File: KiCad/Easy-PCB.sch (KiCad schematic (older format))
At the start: 1 part, among them J3 HLW20R-2C7LF

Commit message: microcontroller schematic kicad
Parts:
- added C?: 0.1u, symbol C_Small
- added P?: USART, symbol CONN_01X02
- added P?: CONN_01X06, symbol CONN_01X06
- added R? (x8): 320, symbol R
- added R? (x4): 10k, symbol R
- added U?: PIC16F883, symbol PIC16F883
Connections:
- net Heat Relay/DoorC1: now also J3.19 (P19)
- net Heat Relay/DoorC2: now also J3.20 (P20)
- net Heat Relay/Heat: now also U?.5 (RA3/AN3/Vref+/C1IN+)
- net Temperature Feedback/Tk: now also U?.2 (RA0/AN0/ULPWU/C12IN0-)
- net Temperature Feedback/Tref: now also U?.3 (RA1/AN1/C12IN1-)
- net Temperature Feedback/Vref-: now also U?.4 (RA2/AN2/Vref-/CVref/C2IN+)
- net CS1: now reaches J3.1 (P1)
- net CS1: now also R?.2, U?.7 (RA5/AN4/~SS~/C2OUT)
- net VDD: now reaches J3.10 (P10)
- net VDD: now also J3.8 (P8), J3.9 (P9), C?.2, P?.2 (P2), R?.1, R?.1, R?.1, R?.1, U?.20 (Vdd)
- net at J3.11 (P11): now also R?.2
- net at J3.12 (P12): now also R?.2
- net at J3.13 (P13): now also R?.2
- net at J3.14 (P14): now also R?.2
- net at J3.15 (P15): now also R?.2
- net at J3.16 (P16): now also R?.2
- net at J3.17 (P17): now also R?.2
- net at J3.18 (P18): now also R?.2
- net SCK: now reaches J3.2 (P2)
- net SCK: now also R?.2, U?.14 (RC3/SCK/SCL)
- net MISO: now reaches J3.3 (P3)
- net MISO: now also U?.15 (RC4/SDI/SDA)
- net MOSI: now reaches J3.4 (P4)
- net MOSI: now also U?.16 (RC5/SDO)
- net GND: now reaches J3.5 (P5)
- net GND: now also J3.6 (P6), J3.7 (P7), C?.1, P?.3 (P3), U?.19 (Vss), U?.8 (Vss)
- new net: P?.1 (P1), U?.1 (RE3/~MCLR~/Vpp)
- new net: R?.1, U?.21 (RB0/AN12/INT)
- new net: R?.1, U?.22 (RB1/AN10/P1C/C12IN3-)
- new net: R?.1, U?.23 (RB2/AN8/P1B)
- new net: R?.1, U?.24 (RB3/AN9/PGM/C12IN2-)
- new net: R?.1, U?.25 (RB4/AN11/P1D)
- new net: R?.1, U?.26 (RB5/AN13/~T1G)
- new net: P?.5 (P5), R?.1, U?.27 (RB6/ICSPCLK)
- new net: P?.4 (P4), R?.1, U?.28 (RB7/ICSPDAT)
- new net CS2: R?.2, U?.10 (RA6/OSC2/CLKOUT)
- new net RX: P?.2 (P2), U?.18 (RC7/RX/DT)
- new net TX: P?.1 (P1), U?.17 (RC6/TX/CK)
- no-connect marks 0 -> 1
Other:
- moved on the sheet: J3

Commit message: kicad motor and speaker schematics
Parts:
- added Q?: 2N3904, SOT-23, symbol MMBT3904
- added R? (x2): 1k, symbol R
- added SP?: SPEAKER, symbol SPEAKER
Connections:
- net GND: now also Q?.2 (E)
- net VDD: now also R?.1, SP?.1
- net Motor Driver/Motor_On: now reaches U?.11 (RC0/T1OSO/T1CKI)
- net Motor Driver/wind2: now reaches U?.12 (RC1/T1OSI/CCP2)
- net Motor Driver/wind1: now reaches U?.13 (RC2/P1A/CCP1)
- net at U?.6 (RA4/T0CLI/C1OUT): now also R?.2
- new net: Q?.3 (C), R?.2, SP?.2
- new net: Q?.1 (B), R?.1
- no-connect marks 1 -> 2
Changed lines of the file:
@@
 $Descr USLetter 11000 8500
 encoding utf-8
-Sheet 1 3
+Sheet 1 4
 Title "Easy-PCB-v1"
 Date ""
@@
 	-1   0    0    1
 $EndComp
-Wire Wire Line
-	1600 3600 1200 3600
-Wire Wire Line
-	1600 3700 1200 3700
-Wire Wire Line
-	1600 3800 1200 3800
-Wire Wire Line
-	1200 3900 1600 3900
-Wire Wire Line
-	1200 4000 1600 4000
-Wire Wire Line
-	1200 4100 1600 4100
-Wire Wire Line
-	1200 4200 1600 4200
-Wire Wire Line
-	1200 4300 1600 4300
-Wire Wire Line
-	1900 3700 2800 3700
-Wire Wire Line
-	1900 3800 2800 3800
-Wire Wire Line
-	1900 3900 2800 3900
-Wire Wire Line
-	1900 4000 2800 4000
-Wire Wire Line
-	1900 4100 2800 4100
-Wire Wire Line
-	1900 4200 2800 4200
-Wire Wire Line
-	1900 4300 2800 4300
-Wire Wire Line
-	1900 3600 2700 3600
-Wire Wire Line
-	2700 3600 2700 3500
-Wire Wire Line
-	2700 3500 2800 3500
-Wire Wire Line
-	1200 2900 1500 2900
-Wire Wire Line
-	1500 2900 1500 3000
-Wire Wire Line
-	1500 3000 2800 3000
-Wire Wire Line
-	1200 3100 2150 3100
-Wire Wire Line
-	1300 3500 1200 3500
-Wire Wire Line
-	1300 3300 1300 3500
-Connection ~ 1300 3400
-Wire Wire Line
-	1300 3300 1200 3300
-Wire Wire Line
-	1300 3200 1200 3200
-Wire Wire Line
-	1300 3000 1300 3200
-Connection ~ 1300 3100
-Wire Wire Line
-	1200 3000 1300 3000
-Wire Wire Line
-	2800 3300 2150 3300
-Wire Wire Line
-	2150 3300 2150 3100
-Connection ~ 2000 3100
-Wire Wire Line
-	1200 3400 2800 3400
-Connection ~ 1500 3400
-Wire Wire Line
-	1700 3150 1700 3100
-Connection ~ 1700 3100
-Wire Wire Line
-	1700 3350 1700 3400
-Connection ~ 1700 3400
-Wire Wire Line
-	1200 2800 1900 2800
-Wire Wire Line
-	1900 2800 1900 2900
-Wire Wire Line
-	1900 2900 2800 2900
-Wire Wire Line
-	2600 2000 2600 3200
-Wire Wire Line
-	2600 3200 2800 3200
-Wire Wire Line
-	2500 2000 2500 3100
-Wire Wire Line
-	2500 3100 2800 3100
-Wire Wire Line
-	5300 3500 5450 3500
-Wire Wire Line
-	5600 3700 5300 3700
-Wire Wire Line
-	5600 2200 5600 3700
-Wire Wire Line
-	5600 2600 1200 2600
-Wire Wire Line
-	1200 2700 5300 2700
-Wire Wire Line
-	5300 2200 5300 2900
-Wire Wire Line
-	5300 4200 5800 4200
-Wire Wire Line
-	5300 4100 5700 4100
-Wire Wire Line
-	5300 4000 5600 4000
-Wire Wire Line
-	5600 4000 5600 5600
-Wire Wire Line
-	5600 5600 6300 5600
-Wire Wire Line
-	5700 4100 5700 5500
-Wire Wire Line
-	5700 5500 6300 5500
-Wire Wire Line
-	5800 4200 5800 5400
-Wire Wire Line
-	5800 5400 6300 5400
-Wire Wire Line
-	8100 4600 1500 4600
-Wire Wire Line
-	1500 4600 1500 4400
-Wire Wire Line
-	1500 4400 1200 4400
-Wire Wire Line
-	8100 4700 1200 4700
-Wire Wire Line
-	1200 4700 1200 4500
-Wire Wire Line
-	5300 3900 6100 3900
-Wire Wire Line
-	6100 3900 6100 4450
-Wire Wire Line
-	6100 4450 8100 4450
-Wire Wire Line
-	6300 5900 5150 5900
-Wire Wire Line
-	6300 6050 5150 6050
-Wire Wire Line
-	5300 3300 5900 3300
-Wire Wire Line
-	5900 2200 5900 5750
-Wire Wire Line
-	5900 5750 6300 5750
-Connection ~ 5300 2700
-Connection ~ 5600 2600
-Connection ~ 5900 3300
-Wire Wire Line
-	5300 1900 5300 1800
-Wire Wire Line
-	5300 1800 5900 1800
-Wire Wire Line
-	5900 1800 5900 1900
-Wire Wire Line
-	5600 1650 5600 1900
-Connection ~ 5600 1800
-Wire Wire Line
-	2400 2050 2500 2050
-Connection ~ 2500 2050
-Wire Wire Line
-	2600 2050 2700 2050
-Connection ~ 2600 2050
-Wire Wire Line
-	2800 5500 5300 5500
-Wire Wire Line
-	5300 5500 5300 4300
-Connection ~ 3300 5500
-Wire Wire Line
-	3300 5050 3300 5150
-Wire Wire Line
-	2700 5500 2700 5100
-Wire Wire Line
-	2700 5100 3300 5100
-Connection ~ 3300 5100
-Wire Wire Line
-	2600 5500 2600 5300
 $Comp
 L CONN_01X06 P?
@@
 $EndComp
 NoConn ~ 2300 5500
+$Comp
+L SPEAKER SP?
+U 1 1 56815E3D
+P 7550 3600
+F 0 "SP?" H 7450 3850 50  0000 C CNN
+F 1 "SPEAKER" H 7450 3350 50  0000 C CNN
+F 2 "" H 7550 3600 50  0000 C CNN
+F 3 "" H 7550 3600 50  0000 C CNN
+	1    7550 3600
+	1    0    0    -1
+$EndComp
+$Comp
+L MMBT3904 Q?
+U 1 1 56815FFA
+P 6900 4000
+F 0 "Q?" H 7100 4075 50  0000 L CNN
+F 1 "2N3904" H 7100 4000 50  0000 L CNN
+F 2 "SOT-23" H 7100 3925 50  0000 L CIN
+F 3 "" H 6900 4000 50  0000 L CNN
+	1    6900 4000
+	1    0    0    -1
+$EndComp
+$Comp
+L R R?
+U 1 1 56816949
+P 6800 3600
+F 0 "R?" V 6880 3600 50  0000 C CNN
+F 1 "1k" V 6800 3600 50  0000 C CNN
+F 2 "" V 6730 3600 50  0000 C CNN
+F 3 "" H 6800 3600 50  0000 C CNN
+	1    6800 3600
+	1    0    0    -1
+$EndComp
+$Comp
+L R R?
+U 1 1 568169CA
+P 6350 3800
+F 0 "R?" V 6430 3800 50  0000 C CNN
+F 1 "1k" V 6350 3800 50  0000 C CNN
+F 2 "" V 6280 3800 50  0000 C CNN
+F 3 "" H 6350 3800 50  0000 C CNN
+	1    6350 3800
+	0    1    1    0
+$EndComp
+$Comp
+L GND #PWR?
+U 1 1 56816B80
+P 7000 4200
+F 0 "#PWR?" H 7000 3950 50  0001 C CNN
+F 1 "GND" H 7000 4050 50  0000 C CNN
+F 2 "" H 7000 4200 50  0000 C CNN
+F 3 "" H 7000 4200 50  0000 C CNN
+	1    7000 4200
+	1    0    0    -1
+$EndComp
+$Comp
+L VDD #PWR?
+U 1 1 56816C00
+P 7000 3450
+F 0 "#PWR?" H 7000 3300 50  0001 C CNN
+F 1 "VDD" H 7000 3600 50  0000 C CNN
+F 2 "" H 7000 3450 50  0000 C CNN
+F 3 "" H 7000 3450 50  0000 C CNN
+	1    7000 3450
+	1    0    0    -1
+$EndComp
+Wire Wire Line
+	1600 3600 1200 3600
+Wire Wire Line
+	1600 3700 1200 3700
+Wire Wire Line
+	1600 3800 1200 3800
+Wire Wire Line
+	1200 3900 1600 3900
+Wire Wire Line
+	1200 4000 1600 4000
+Wire Wire Line
+	1200 4100 1600 4100
+Wire Wire Line
+	1200 4200 1600 4200
+Wire Wire Line
+	1200 4300 1600 4300
+Wire Wire Line
+	1900 3700 2800 3700
+Wire Wire Line
+	1900 3800 2800 3800
+Wire Wire Line
+	1900 3900 2800 3900
+Wire Wire Line
+	1900 4000 2800 4000
+Wire Wire Line
+	1900 4100 2800 4100
+Wire Wire Line
+	1900 4200 2800 4200
+Wire Wire Line
+	1900 4300 2800 4300
+Wire Wire Line
+	1900 3600 2700 3600
+Wire Wire Line
+	2700 3600 2700 3500
+Wire Wire Line
+	2700 3500 2800 3500
+Wire Wire Line
+	1200 2900 1500 2900
+Wire Wire Line
+	1500 2900 1500 3000
+Wire Wire Line
+	1500 3000 2800 3000
+Wire Wire Line
+	1200 3100 2150 3100
+Wire Wire Line
+	1300 3500 1200 3500
+Wire Wire Line
+	1300 3300 1300 3500
+Connection ~ 1300 3400
+Wire Wire Line
+	1300 3300 1200 3300
+Wire Wire Line
+	1300 3200 1200 3200
+Wire Wire Line
+	1300 3000 1300 3200
+Connection ~ 1300 3100
+Wire Wire Line
+	1200 3000 1300 3000
+Wire Wire Line
+	2800 3300 2150 3300
+Wire Wire Line
+	2150 3300 2150 3100
+Connection ~ 2000 3100
+Wire Wire Line
+	1200 3400 2800 3400
+Connection ~ 1500 3400
+Wire Wire Line
+	1700 3150 1700 3100
+Connection ~ 1700 3100
+Wire Wire Line
+	1700 3350 1700 3400
+Connection ~ 1700 3400
+Wire Wire Line
+	1200 2800 1900 2800
+Wire Wire Line
+	1900 2800 1900 2900
+Wire Wire Line
+	1900 2900 2800 2900
+Wire Wire Line
+	2600 2000 2600 3200
+Wire Wire Line
+	2600 3200 2800 3200
+Wire Wire Line
+	2500 2000 2500 3100
+Wire Wire Line
+	2500 3100 2800 3100
+Wire Wire Line
+	5300 3500 5450 3500
+Wire Wire Line
+	5600 3700 5300 3700
+Wire Wire Line
+	5600 2200 5600 3700
+Wire Wire Line
+	5600 2600 1200 2600
+Wire Wire Line
+	1200 2700 5300 2700
+Wire Wire Line
+	5300 2200 5300 2900
+Wire Wire Line
+	5300 4200 5800 4200
+Wire Wire Line
+	5300 4100 5700 4100
+Wire Wire Line
+	5300 4000 5600 4000
+Wire Wire Line
+	5600 4000 5600 5600
+Wire Wire Line
+	5600 5600 6300 5600
+Wire Wire Line
+	5700 4100 5700 5500
+Wire Wire Line
+	5700 5500 6300 5500
+Wire Wire Line
+	5800 4200 5800 5400
+Wire Wire Line
+	5800 5400 6300 5400
+Wire Wire Line
+	8100 4600 1500 4600
+Wire Wire Line
+	1500 4600 1500 4400
+Wire Wire Line
+	1500 4400 1200 4400
+Wire Wire Line
+	8100 4700 1200 4700
+Wire Wire Line
+	1200 4700 1200 4500
+Wire Wire Line
+	5300 3900 6100 3900
+Wire Wire Line
+	6100 3900 6100 4450
+Wire Wire Line
+	6100 4450 8100 4450
+Wire Wire Line
+	6300 5900 5150 5900
+Wire Wire Line
+	6300 6050 5150 6050
+Wire Wire Line
+	5300 3300 5900 3300
+Wire Wire Line
+	5900 2200 5900 5750
+Wire Wire Line
+	5900 5750 6300 5750
+Connection ~ 5300 2700
+Connection ~ 5600 2600
+Connection ~ 5900 3300
+Wire Wire Line
+	5300 1900 5300 1800
+Wire Wire Line
+	5300 1800 5900 1800
+Wire Wire Line
+	5900 1800 5900 1900
+Wire Wire Line
+	5600 1650 5600 1900
+Connection ~ 5600 1800
+Wire Wire Line
+	2400 2050 2500 2050
+Connection ~ 2500 2050
+Wire Wire Line
+	2600 2050 2700 2050
+Connection ~ 2600 2050
+Wire Wire Line
+	2800 5500 5300 5500
+Wire Wire Line
+	5300 5500 5300 4300
+Connection ~ 3300 5500
+Wire Wire Line
+	3300 5050 3300 5150
+Wire Wire Line
+	2700 5500 2700 5100
+Wire Wire Line
+	2700 5100 3300 5100
+Connection ~ 3300 5100
+Wire Wire Line
+	2600 5500 2600 5300
 Wire Wire Line
 	2400 5500 2400 4200
@@
 	2500 5500 2500 4300
 Connection ~ 2500 4300
+Wire Wire Line
+	6800 3450 7000 3450
+Wire Wire Line
+	7000 3450 7000 3500
+Wire Wire Line
+	7000 3500 7250 3500
+Wire Wire Line
+	6800 3750 7000 3750
+Wire Wire Line
+	7000 3700 7000 3800
+Wire Wire Line
+	7000 3700 7250 3700
+Connection ~ 7000 3750
+Wire Wire Line
+	5300 3800 6200 3800
+Wire Wire Line
+	6500 3800 6600 3800
+Wire Wire Line
+	6600 3800 6600 4000
+Wire Wire Line
+	6600 4000 6700 4000
+$Sheet
+S 8100 2900 1000 500
+U 5681BEC8
+F0 "Motor Driver" 60
+F1 "Motor-Driver.sch" 60
+F2 "wind1a" O R 9100 3000 60
+F3 "wind1b" O R 9100 3100 60
+F4 "wind2a" O R 9100 3200 60
+F5 "wind2b" O R 9100 3300 60
+F6 "wind1" I L 8100 3000 60
+F7 "wind2" I L 8100 3100 60
+F8 "Motor_On" I L 8100 3200 60
+$EndSheet
+Wire Wire Line
+	5300 3200 8100 3200
+Wire Wire Line
+	5300 3100 8100 3100
+Wire Wire Line
+	5300 3000 8100 3000
+NoConn ~ 5300 3400
 $EndSCHEMATC

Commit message: power circuit schematic in kicad
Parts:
- added C?: CP1, symbol CP1
- added J?: IEC Male Inlet: 703W-00/53, symbol IEC_Male_Inlet
- added P?: Molex 0022032041, symbol CONN_01X04
- added R? (x2): R, symbol R
- added SW?: SPST: DF62J12S2AHQA, symbol SPST
- P?: value USART -> Molex 0022032021
- P?: value CONN_01X06 -> Molex 0901200126
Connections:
- net GND: now also J?.3 (Neutral)
- net Heat Relay/Heat: now also U?.6 (RA4/T0CLI/C1OUT); no longer U?.5 (RA3/AN3/Vref+/C1IN+)
- net Motor Driver/wind1a: now also P?.1 (P1)
- net Motor Driver/wind1b: now also P?.2 (P2)
- net Motor Driver/wind2a: now also P?.3 (P3)
- net Motor Driver/wind2b: now also P?.4 (P4)
- net Temperature Feedback/Vref-: now also C?.2, R?.2
- net at R?.2: now also U?.9 (RA7/OSC1/CLKIN); no longer U?.6 (RA4/T0CLI/C1OUT)
- new net: R?.2, U?.5 (RA3/AN3/Vref+/C1IN+)
- new net: J?.1 (Live), SW?.1
- new net: C?.1, R?.1, R?.1
- new net Earth: J?.2 (Earth)
- new net Power Circuit/MainsLive: SW?.2
- no-connect marks 2 -> 1
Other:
- moved on the sheet: Q?, R?, SP?

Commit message: controller board schematic complete
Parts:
- removed C?: CP1, symbol CP1
- removed R? (x2): R, symbol R
- added P4: Molex 387203208, symbol CONN_01X03
- added P5: Molex 0022032021, symbol CONN_01X02
- added R9: 320, symbol R
- gave numbers to parts that had none: 23
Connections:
- net Earth: now also P4.3 (P3)
- net GND: now also P4.2 (P2), P5.2 (P2)
- net Heat Relay/HeatLive: now also P4.1 (P1)
- net Temperature Feedback/K+: now also P5.1 (P1)
- net VDD: no longer J3.10 (P10)
- net at R1.2: now also J3.10 (P10); no longer J3.11 (P11)
- net at R2.2: now also J3.11 (P11); no longer J3.12 (P12)
- net at R3.2: now also J3.12 (P12); no longer J3.13 (P13)
- net at R4.2: now also J3.13 (P13); no longer J3.14 (P14)
- net at R5.2: now also J3.14 (P14); no longer J3.15 (P15)
- net at R6.2: now also J3.15 (P15); no longer J3.16 (P16)
- net at R7.2: now also J3.16 (P16); no longer J3.17 (P17)
- net at R8.2: now also J3.17 (P17); no longer J3.18 (P18)
- net at P2.1 (P1), U1.1 (RE3/~MCLR~/Vpp): now also R9.1
- net Analog Math/NichromeTemp: now reaches U1.5 (RA3/AN3/Vref+/C1IN+)
- net Heat Relay/Heat renamed Analog Math/Heat
- new net: J3.18 (P18), R9.2
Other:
- moved on the sheet: J3, P2, Q1, R10, R14, R15, SP1

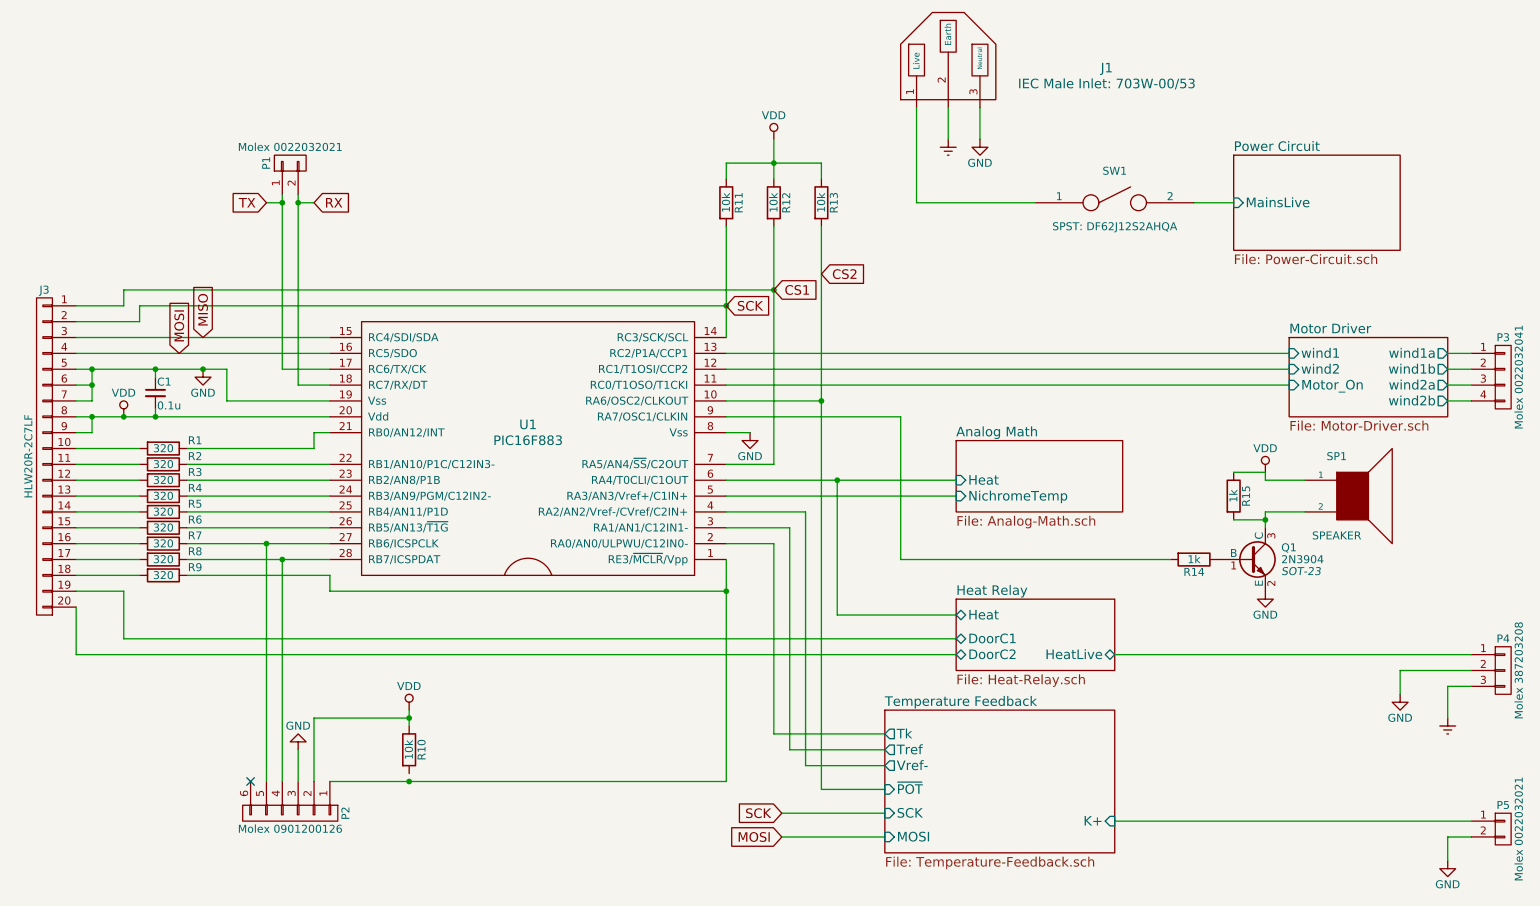
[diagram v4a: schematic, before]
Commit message: HeatOn fix, replaced R1-8 with array
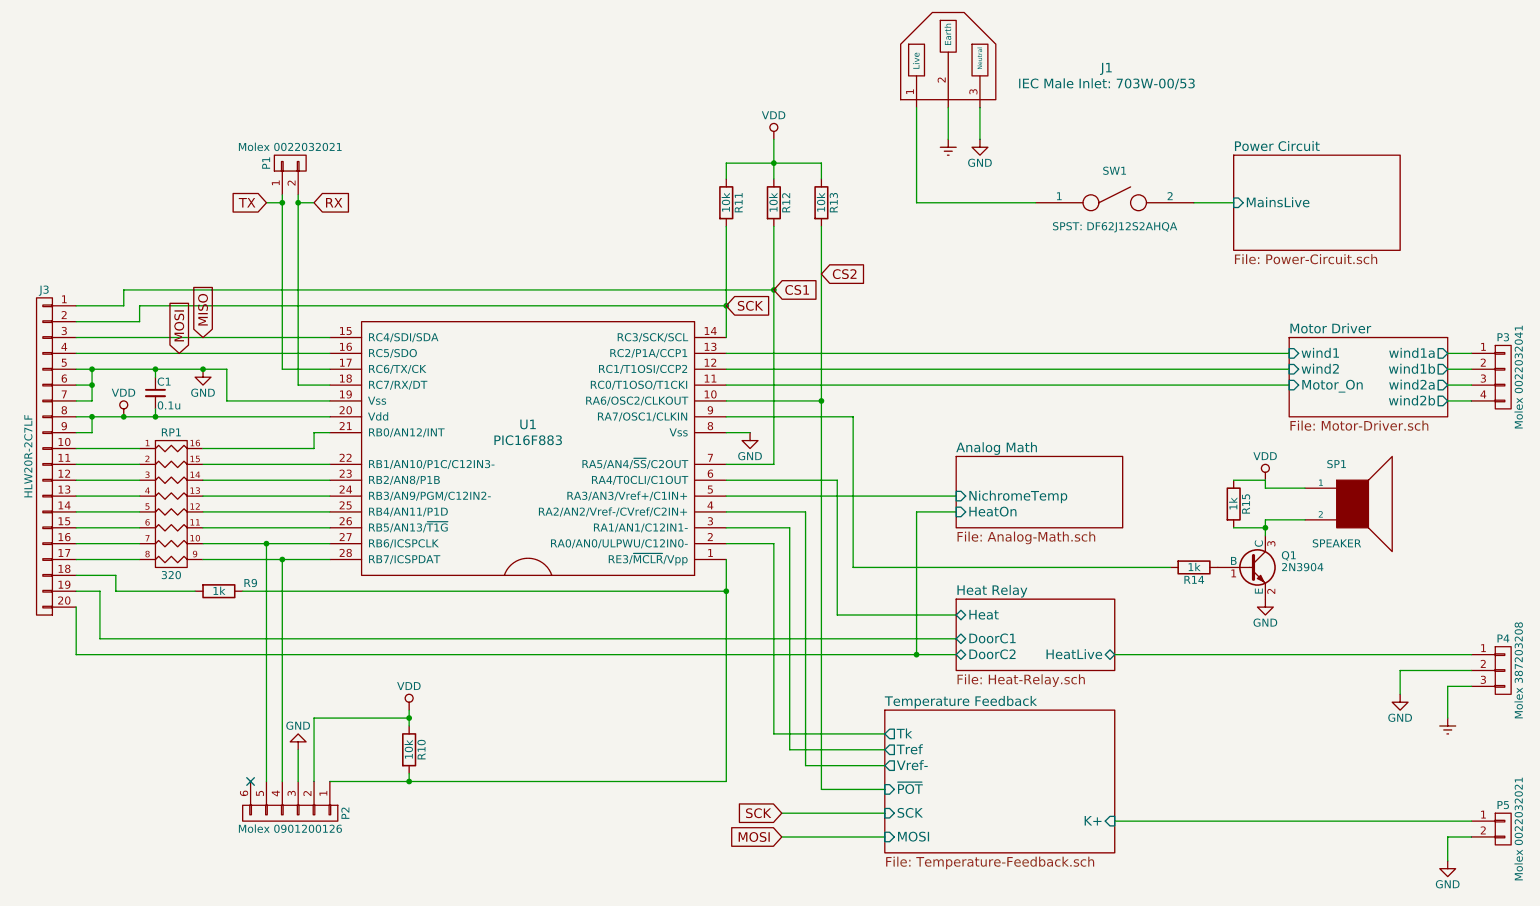
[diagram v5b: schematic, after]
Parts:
- removed R1, R2, R3, R4, R5, R6, R7, R8: 320, symbol R
- added RP1: 320, symbol R_PACK8
- Q1: footprint SOT-23 -> (none)
- R9: value 320 -> 1k
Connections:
- net at J3.10 (P10): now also RP1.1 (P1)
- net at J3.11 (P11): now also RP1.2 (P2)
- net at J3.12 (P12): now also RP1.3 (P3)
- net at J3.13 (P13): now also RP1.4 (P4)
- net at J3.14 (P14): now also RP1.5 (P5)
- net at J3.15 (P15): now also RP1.6 (P6)
- net at J3.16 (P16): now also RP1.7 (P7)
- net at J3.17 (P17): now also RP1.8 (P8)
- net at P2.1 (P1), R9.1, U1.1 (RE3/~MCLR~/Vpp): now also R10.2
- net at U1.21 (RB0/AN12/INT): now also RP1.16 (R1)
- net at U1.22 (RB1/AN10/P1C/C12IN3-): now also RP1.15 (R2)
- net at U1.23 (RB2/AN8/P1B): now also RP1.14 (R3)
- net at U1.24 (RB3/AN9/PGM/C12IN2-): now also RP1.13 (R4)
- net at U1.25 (RB4/AN11/P1D): now also RP1.12 (R5)
- net at U1.26 (RB5/AN13/~T1G): now also RP1.11 (R6)
- net at P2.5 (P5), U1.27 (RB6/ICSPCLK): now also RP1.10 (R7)
- net at P2.4 (P4), U1.28 (RB7/ICSPDAT): now also RP1.9 (R8)
- net Analog Math/Heat renamed Heat Relay/Heat
- net Heat Relay/DoorC2 renamed Analog Math/HeatOn
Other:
- moved on the sheet: Q1, R14, R15, R9, SP1
